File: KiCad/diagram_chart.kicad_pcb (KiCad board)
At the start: 2 copper layers, 160 x 160 mm, 79 parts, among them SW0 SW0, SW1 SW1, SW2 SW2, SW3 SW3, SW4 SW4, SW5 SW5, SW6 SW6, SW7 SW7, U1 TPIC6C595, U2 74HC165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

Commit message: Changed from A3 to A4.
Will make it easier to print PCB and check footprints before ordering.
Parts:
- moved C1 114.6 mm to (137.9, 162.0)
- moved C2 114.6 mm to (137.9, 165.2)
- moved CU1 114.6 mm to (137.9, 168.3)
- moved CU_Caps1 114.6 mm to (137.9, 171.5)
- moved C_MCU1 114.6 mm to (92.0, 169.1)
- moved D3 114.6 mm to (83.4, 87.6)
- moved D4 114.6 mm to (135.9, 87.6)
- moved D5 114.6 mm to (143.5, 87.6)
- moved D6 114.6 mm to (151.1, 87.6)
- moved D7 114.6 mm to (158.8, 87.6)
- moved D8 114.6 mm to (111.3, 171.7)
- moved DC-In1 114.6 mm to (43.4, 68.2)
- moved F1 114.6 mm to (110.8, 164.4)
- moved PWR_Screw1 114.6 mm to (35.6, 151.1)
- moved R10 114.6 mm to (102.4, 109.0)
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
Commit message: Made 14x14 cm. Positioned and alligned switches, displays and LEDs. 1oZ coppar makes me decide for 1mm width per AMP Meaning 0,2mm is enough for 200mA
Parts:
- D0, D1, D2, D3, D4, D5, D6, D7: footprint LED_THT:LED_D5.0mm -> LED_THT:LED_D3.0mm
- moved C_MCU1 148.6 mm to (-56.1, 157.3)
- moved F1 148.6 mm to (-37.3, 152.6)
- moved R1 148.6 mm to (-56.4, 95.3)
- moved R10 148.6 mm to (-45.7, 97.1)
- moved R11 148.6 mm to (-45.7, 100.3)
- moved R12 148.6 mm to (-45.7, 103.4)
- moved R13 148.6 mm to (-45.7, 106.6)
- moved R14 148.6 mm to (-45.7, 109.7)
- moved R15 148.6 mm to (-45.7, 112.9)
- moved R16 148.6 mm to (-45.7, 116.0)
- moved R17 148.6 mm to (-45.7, 119.2)
- moved R18 148.6 mm to (-63.8, 150.9)
- moved R19 148.6 mm to (-63.8, 154.0)
- moved R2 148.6 mm to (-56.4, 99.4)
- moved R20 148.6 mm to (-63.8, 157.2)
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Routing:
- net Net-(T_DEC_2-E): track 0.00 -> 59.4 mm
- net Net-(T_DEC_1-E): track 0.00 -> 57.0 mm
- net Net-(T_DEC_0-E): track 0.00 -> 52.4 mm
- net Net-(D8-K): track 0.00 -> 28.6 mm
- net Net-(T_HEX_0-E): track 0.00 -> 21.8 mm
- net Net-(T_HEX_1-E): track 0.00 -> 21.6 mm
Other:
- board size 160 x 160 mm -> 140 x 140 mm

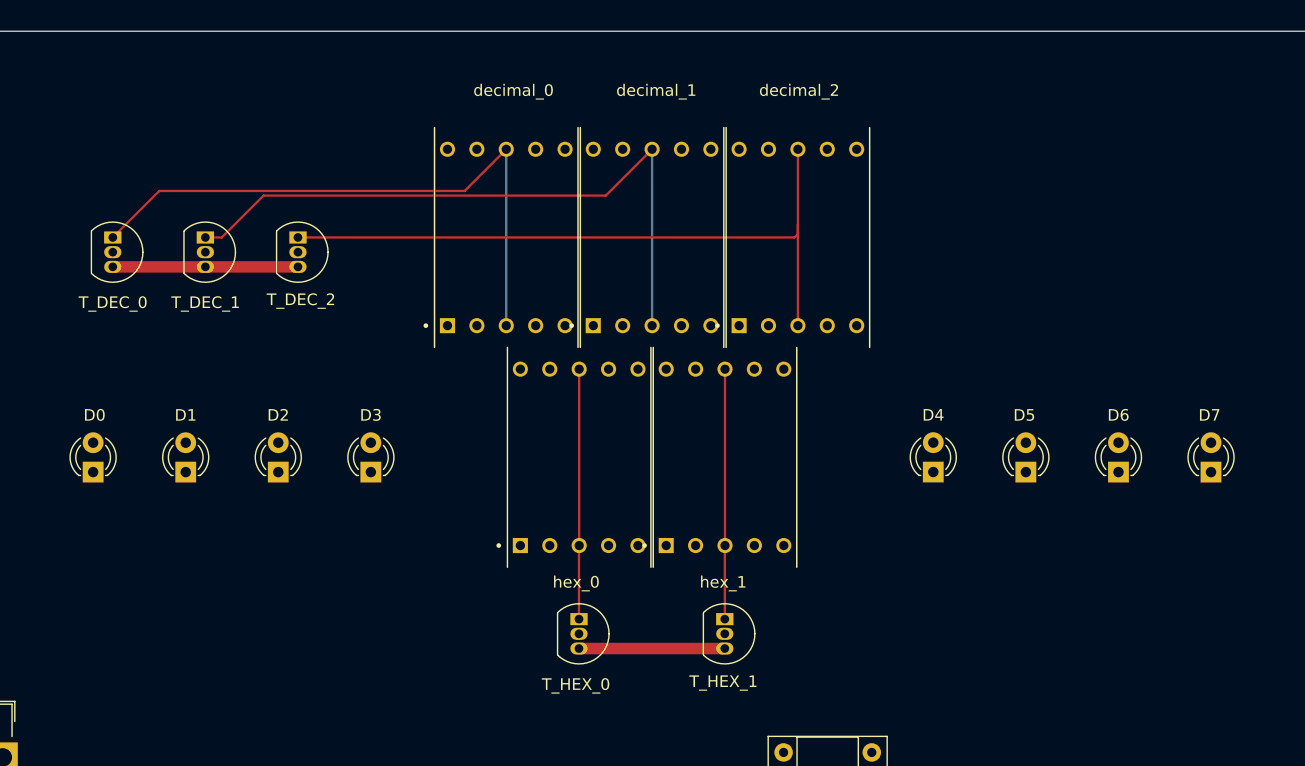
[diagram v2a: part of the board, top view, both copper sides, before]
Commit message: Centered the displays to middle Also grouped the entire section
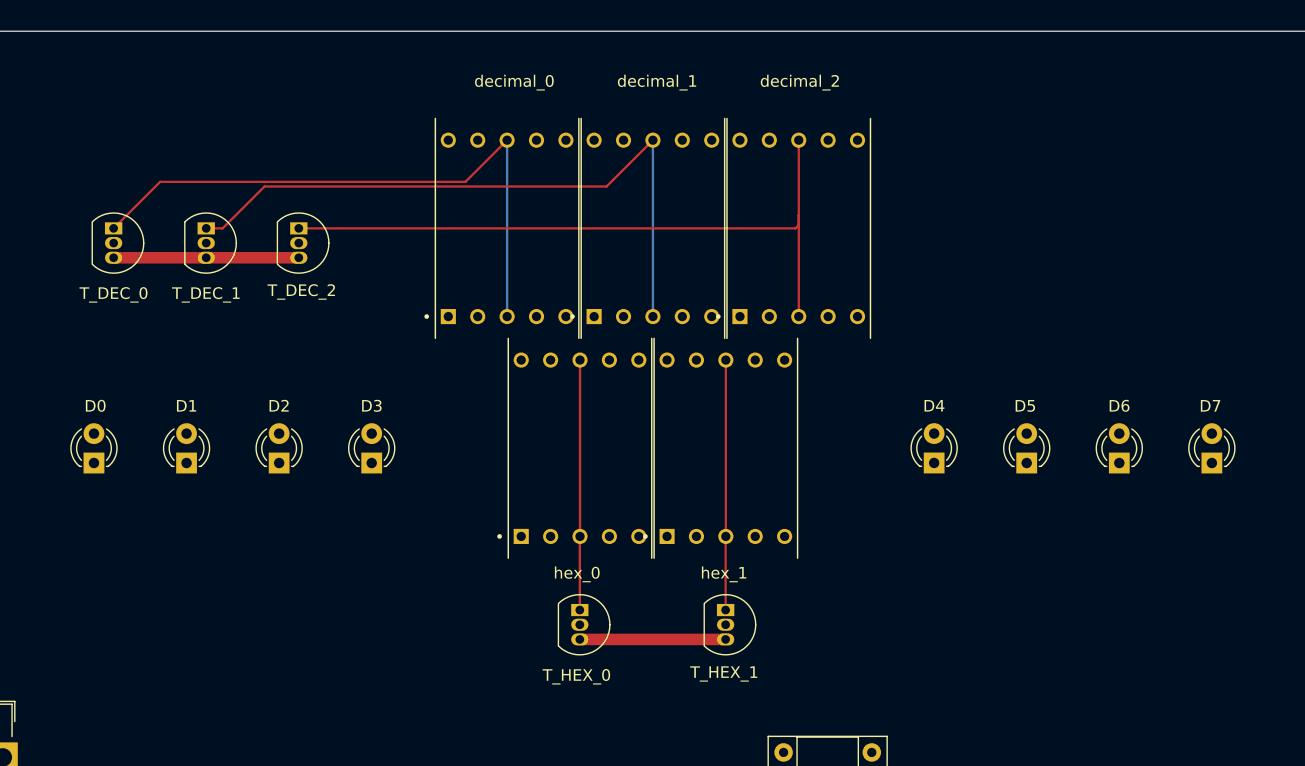
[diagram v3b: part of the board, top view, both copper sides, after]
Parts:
- moved T_DEC_0 0.79 mm to (64.0, 67.8)
- moved T_DEC_1 0.79 mm to (72.0, 67.8)
- moved T_DEC_2 0.79 mm to (80.0, 67.8)
- moved decimal_0 0.79 mm to (98.0, 67.8)
- moved decimal_1 0.79 mm to (110.6, 67.8)
- moved hex_0 0.79 mm to (104.3, 86.8)
- moved decimal_2 0.79 mm to (123.2, 67.8)
- moved hex_1 0.79 mm to (116.9, 86.8)
- moved D1 0.79 mm to (70.3, 88.1)
- moved D2 0.79 mm to (78.3, 88.1)
- moved D3 0.79 mm to (86.3, 88.1)
- moved D4 0.79 mm to (134.9, 88.1)
- moved D5 0.79 mm to (142.9, 88.1)
- moved D6 0.79 mm to (150.9, 88.1)
- moved D7 0.79 mm to (158.9, 88.1)
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
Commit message: Added traces, and a lot of VIAS. Not certain about distances from pads, but expensive lessons are the best stucking ones.
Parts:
- added ?: , , F.Cu at (93.6, 134.9)
- added ?: , , F.Cu at (92.4, 113.5)
- added ?: , , F.Cu at (87.3, 113.5)
- added ?: , , F.Cu at (120.0, 127.5)
- added ?: , , F.Cu at (88.5, 134.9)
- moved R7 217.0 mm to (158.9, 92.6), turned to -90 degrees
- moved R6 208.6 mm to (150.9, 92.6), turned to -90 degrees
- moved R5 200.2 mm to (142.9, 92.6), turned to -90 degrees
- moved R4 191.9 mm to (134.9, 92.6), turned to -90 degrees
- moved R3 143.1 mm to (86.3, 92.6), turned to -90 degrees
- moved Serial_Screw1 141.6 mm to (177.0, 136.6), turned to 90 degrees
- moved R2 134.9 mm to (78.3, 92.6), turned to -90 degrees
- moved R1 126.7 mm to (70.3, 92.6), turned to -90 degrees
- moved RGB1 124.4 mm to (177.0, 126.6), turned to 90 degrees
- moved C1 123.0 mm to (230.4, 136.3)
- moved C2 123.0 mm to (222.2, 134.1)
- moved F1 103.5 mm to (58.6, 113.5)
- moved D8 80.3 mm to (82.2, 119.6), turned to -90 degrees
- moved R0 57.3 mm to (62.3, 92.6), turned to -90 degrees
- moved U_Caps1 19.3 mm to (237.5, 78.1), turned to 180 degrees
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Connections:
- D8 pad 1: Net-(D8-K) -> Net-(U1-DRAIN0)
- F1 pad 2: Net-(D8-K) -> Net-(U1-DRAIN0)
- PWR_Screw1 pad 1: Net-(D8-K) -> Net-(U1-DRAIN0)
- T_DEC_0 pad 1: Net-(T_DEC_0-E) -> Net-(D0-A)
- T_HEX_0 pad 3: Net-(D8-K) -> Net-(U1-DRAIN0)
- T_HEX_1 pad 3: Net-(D8-K) -> Net-(U1-DRAIN0)
- T_LED1 pad 2: Net-(T_LED1-B) -> Net-(D0-A)
- T_LED1 pad 3: Net-(D8-K) -> Net-(D0-A)
- U1 pad 1: Net-(D8-K) -> Net-(U1-DRAIN0)
- decimal_0 pad 3: Net-(T_DEC_0-E) -> Net-(D0-A)
- decimal_0 pad 8: Net-(T_DEC_0-E) -> Net-(D0-A)
- decimal_2 pad 6: Net-(D1-K) -> Net-(D0-A)
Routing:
- net Net-(D0-A): track 0.00 -> 269.3 mm
- net Net-(U1-DRAIN0): track 0.00 -> 226.6 mm
- net Net-(D5-K): track 0.00 -> 161.0 mm, vias 0 -> 4
- net GND: track 0.00 -> 150.0 mm
- net Net-(D0-K): track 0.00 -> 128.6 mm, vias 0 -> 3
- net Net-(D4-K): track 0.00 -> 124.7 mm, vias 0 -> 2
- net Net-(D2-K): track 0.00 -> 124.5 mm, vias 0 -> 2
- net Net-(D1-K): track 0.00 -> 123.6 mm, vias 0 -> 5
- net Net-(D7-K): track 0.00 -> 119.7 mm, vias 0 -> 3
- net Net-(D6-K): track 0.00 -> 119.4 mm, vias 0 -> 2
- net Net-(U1-DRAIN1): track 0.00 -> 78.7 mm
- net Net-(D3-K): track 0.00 -> 70.5 mm, vias 0 -> 1
- net Net-(U1-DRAIN2): track 0.00 -> 67.5 mm
- net Net-(U1-DRAIN3): track 0.00 -> 56.8 mm
- net Net-(T_DEC_0-E): track 52.4 -> 0.00 mm
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
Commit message: Fixed SPDT to correct sizes. Also flipped them so down is off. Added values of resistors, etc to silkscreen. Made the board 13x13 instead of 14x14. Centralized SPDT sw3, will after lunch center the rest accordingly.
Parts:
- SW0, SW1, SW2, SW3, SW4, SW5, SW6, SW7, SW_Mem1, SW_Serr1, SW__WR1: footprint switch:SW_Toggle_Blue_wSlots -> switch:SW_Toggle_Blue_SMALL
- moved ? 17.8 mm to (88.0, 118.0), turned to 90 degrees
- moved ? 11.8 mm to (88.0, 123.1), turned to 90 degrees
- moved U2 10.0 mm to (106.8, 154.7)
- moved SW3 8.43 mm to (95.7, 170.0), turned to -90 degrees
- moved Serial_Screw1 0.50 mm to (176.5, 136.5)
- moved RGB1 0.50 mm to (176.5, 126.5)
- moved ? 0.50 mm to (92.9, 113.5)
- moved ? 0.50 mm to (87.8, 113.5)
- moved D8 0.50 mm to (82.7, 119.6)
- moved DC-In1 0.50 mm to (55.0, 113.5)
- moved F1 0.50 mm to (59.1, 113.5)
- moved PWR_Screw1 0.50 mm to (54.1, 124.4)
- turned SW0 to -90 degrees
- turned SW1 to -90 degrees
- turned SW2 to -90 degrees
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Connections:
- D8 pad 1: Net-(U1-DRAIN0) -> Net-(D8-K)
- F1 pad 2: Net-(U1-DRAIN0) -> Net-(D8-K)
- PWR_Screw1 pad 1: Net-(U1-DRAIN0) -> Net-(D8-K)
- SW_Mem1 pad 3: unconnected-(SW_Mem1-C-Pad3) -> Net-(D8-K)
- SW__WR1 pad 3: unconnected-(SW__WR1-C-Pad3) -> Net-(D8-K)
- T_DEC_0 pad 1: Net-(D0-A) -> Net-(T_DEC_0-E)
- T_HEX_0 pad 3: Net-(U1-DRAIN0) -> Net-(D8-K)
- T_HEX_1 pad 3: Net-(U1-DRAIN0) -> Net-(D8-K)
- T_LED1 pad 2: Net-(D0-A) -> Net-(T_LED1-B)
- T_LED1 pad 3: Net-(D0-A) -> Net-(D8-K)
- U1 pad 1: Net-(U1-DRAIN0) -> Net-(D8-K)
- decimal_0 pad 3: Net-(D0-A) -> Net-(T_DEC_0-E)
- decimal_0 pad 8: Net-(D0-A) -> Net-(T_DEC_0-E)
- decimal_2 pad 6: Net-(D0-A) -> Net-(D1-K)
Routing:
- net GND: track 150.0 -> 142.8 mm
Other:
- board size 140 x 140 mm -> 139 x 130 mm

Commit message: Will need to recheck ignored violations tomorrow. DRC checker seems fine. Hole PTH to copper is fine at 0.35mm, not at 0,55. But YOLO
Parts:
- removed the ? at (88.0, 118.0)
- removed the ? at (92.9, 113.5)
- removed the ? at (87.8, 113.5)
- removed the ? at (88.0, 123.1)
- added ?: , , F.Cu at (112.7, 122.5)
- added ?: , , F.Cu at (143.0, 148.2)
- added ?: , , F.Cu at (140.5, 148.2)
- added ?: , , F.Cu at (87.7, 113.5)
- added ?: , , F.Cu at (92.5, 134.3)
- added ?: , , F.Cu at (59.1, 107.5)
- added ?: , , F.Cu at (99.5, 119.8)
- added ?: , , F.Cu at (90.0, 134.3)
- added ?: , , F.Cu at (64.2, 107.5)
- added ?: , , F.Cu at (112.7, 125.0)
- added ?: , , F.Cu at (166.3, 81.0)
- added ?: , , F.Cu at (148.1, 148.2)
- added ?: , , F.Cu at (153.2, 148.2)
- added ?: , , F.Cu at (150.6, 148.2)
- added ?: , , F.Cu at (145.5, 148.2)
- added ?: , , F.Cu at (90.2, 113.5)
- added CU2: 100nF, Capacitor_THT:C_Disc_D3.0mm_W1.6mm_P2.50mm, F.Cu at (135.4, 148.2)
- added R32: 330Ω, Resistor_THT:R_Axial_DIN0207_L6.3mm_D2.5mm_P7.62mm_Horizontal, F.Cu at (166.3, 92.6)
- F1: value 1A -> 2A
- R0, R1, R2, R3, R4, R5, R6, R7: value 220Ω -> 330Ω
- SW_Mem1: value SW__Mem1 -> SW__MEM
- SW__WR1: value SW__WR1 -> SW__WR
- moved R9 208.2 mm to (158.4, 135.0), turned to 180 degrees
- moved SW_N1 207.2 mm to (150.9, 160.3)
- moved R10 202.3 mm to (147.4, 157.4), turned to 90 degrees
- moved R17 194.8 mm to (145.3, 157.4), turned to 90 degrees
- moved R16 193.3 mm to (143.1, 157.4), turned to 90 degrees
- moved R15 191.9 mm to (141.0, 157.4), turned to 90 degrees
- moved R14 190.6 mm to (138.8, 157.4), turned to 90 degrees
- moved C_MCU1 189.7 mm to (133.5, 153.0)
- moved R21 180.6 mm to (115.7, 140.6), turned to -90 degrees
- moved R20 177.5 mm to (113.1, 143.1), turned to 90 degrees
- moved R31 176.4 mm to (129.9, 148.3), turned to -90 degrees
- moved R30 174.6 mm to (127.8, 148.3), turned to -90 degrees
- moved R25 173.5 mm to (115.8, 110.4), turned to -90 degrees
- moved R29 172.8 mm to (125.6, 148.3), turned to -90 degrees
- moved R22 161.7 mm to (115.7, 131.6), turned to 90 degrees
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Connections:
- MCU_0 pad 21: unconnected-(MCU_0-AREF-Pad21) -> Net-(MCU_0-AREF)
- RGB1 pad 1: Net-(MCU_0-PB2) -> Net-(RGB1-Pin_1)
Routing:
- net Net-(D8-K): track 16.0 -> 534.3 mm
- net GND: track 142.8 -> 399.0 mm
- net Net-(U_Caps1-QC): track 0.00 -> 144.1 mm
- net Net-(U1-DRAIN0): track 226.6 -> 90.0 mm
- net Net-(U_Caps1-QB): track 0.00 -> 129.0 mm
- net Net-(MCU_0-PB2): track 0.00 -> 94.3 mm
- net Net-(MCU_0-PD4): track 0.00 -> 93.3 mm, vias 0 -> 2
- net Net-(MCU_0-PD6): track 0.00 -> 91.1 mm
- net Net-(D0-A): track 269.3 -> 178.7 mm
- net Net-(U_Caps1-QF): track 0.00 -> 86.7 mm
- net Net-(U_Caps1-QA): track 0.00 -> 84.7 mm
- net Net-(MCU_0-PD0): track 0.00 -> 83.6 mm
- net Net-(MCU_0-PD2): track 0.00 -> 82.6 mm
- net Net-(MCU_0-PD1): track 0.00 -> 76.4 mm
- net Net-(SW0-B): track 0.00 -> 61.1 mm, vias 0 -> 1
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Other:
- board size 139 x 130 mm -> 120 x 120 mm
- board text added: "4x 10K"
- board text added: "5V"
- board text added: "5V NonFused"
- board text added: "8x 10K"
- board text added: "GND"
- board text added: "RX"
- board text added: "TX"

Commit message: Verified the footprint seems ok. Ran DRC checker several times.
I can't claim to be certain of of anything, that would be jinxing.
But will cross my fingers and order the PCB this afternoon.
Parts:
- added ?: , , F.Cu at (161.7, 121.6)
- added ?: , , F.Cu at (154.6, 62.4)
- added ?: , , F.Cu at (59.6, 159.0)
- added ?: , , F.Cu at (59.6, 156.5)
- added ?: , , F.Cu at (161.7, 125.6)
- added ?: , , F.Cu at (152.1, 62.4)
- added ?: , , F.Cu at (161.7, 119.0)
- added ?: , , F.Cu at (161.7, 128.1)
- added ?: , , F.Cu at (54.6, 145.9)
- added NC1: Screw Terminal, TerminalBlock_Phoenix:TerminalBlock_Phoenix_MPT-0,5-2-2.54_1x02_P2.54mm_Horizontal, F.Cu at (54.5, 156.5)
- added NC2: Screw Terminal, TerminalBlock_Phoenix:TerminalBlock_Phoenix_MPT-0,5-2-2.54_1x02_P2.54mm_Horizontal, F.Cu at (154.6, 57.3)
- added NC3: Screw Terminal, TerminalBlock_Phoenix:TerminalBlock_Phoenix_MPT-0,5-2-2.54_1x02_P2.54mm_Horizontal, F.Cu at (166.8, 121.6)
- added NC4: Screw Terminal, TerminalBlock_Phoenix:TerminalBlock_Phoenix_MPT-0,5-2-2.54_1x02_P2.54mm_Horizontal, F.Cu at (166.8, 128.1)
- added PWR_Screw2: Screw Terminal, TerminalBlock_Phoenix:TerminalBlock_Phoenix_MPT-0,5-2-2.54_1x02_P2.54mm_Horizontal, F.Cu at (166.8, 115.0)
- added R33: 330Ω, Resistor_THT:R_Axial_DIN0207_L6.3mm_D2.5mm_P7.62mm_Horizontal, F.Cu at (60.5, 139.4)
- added RGB2: Screw Terminal, TerminalBlock_Phoenix:TerminalBlock_Phoenix_MPT-0,5-2-2.54_1x02_P2.54mm_Horizontal, F.Cu at (54.6, 139.4)
- added Serial_Screw1: Screw Terminal, TerminalBlock_Phoenix:TerminalBlock_Phoenix_MPT-0,5-2-2.54_1x02_P2.54mm_Horizontal, F.Cu at (54.5, 149.9)
- F1: footprint Fuse:Fuseholder_Clip-5x20mm_Keystone_3512_Inline_P23.62x7.27mm_D1.02x1.57mm_Horizontal -> Fuse:Fuseholder_Clip-5x20mm_Eaton_1A5601-01_Inline_P20.80x6.76mm_D1.70mm_Horizontal
- moved R24 0.50 mm to (91.8, 102.1)
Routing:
- net Net-(MCU_0-PD0): track 83.6 -> 255.4 mm, vias 0 -> 1
- net Net-(MCU_0-PD1): track 76.4 -> 243.6 mm, vias 0 -> 1
- net Net-(MCU_0-PB2): track 94.3 -> 256.1 mm
- net Net-(D8-K): track 534.3 -> 569.0 mm
- net GND: track 399.0 -> 433.6 mm, vias 0 -> 1
- net Net-(MCU_0-PD4): track 93.3 -> 84.9 mm
- net +5V: track 40.7 -> 34.5 mm
- net Net-(RGB2-Pin_1): track 0.00 -> 5.91 mm
- net unconnected-(NC4-Pin_2-Pad2): track 0.00 -> 5.08 mm
- net unconnected-(NC4-Pin_1-Pad1): track 0.00 -> 5.08 mm
- net unconnected-(NC3-Pin_2-Pad2): track 0.00 -> 5.08 mm
- net unconnected-(NC3-Pin_1-Pad1): track 0.00 -> 5.08 mm
- net unconnected-(NC2-Pin_2-Pad2): track 0.00 -> 5.08 mm
- net unconnected-(NC2-Pin_1-Pad1): track 0.00 -> 5.08 mm
- net unconnected-(NC1-Pin_2-Pad2): track 0.00 -> 5.08 mm
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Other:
- outline, holes or cut-outs redrawn
- board text added: "+5 GND"
- board text added: "NC"
